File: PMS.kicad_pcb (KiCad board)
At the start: 2 copper layers, 175.5 x 87 mm, 182 parts, among them IC2 SI4459ADY-T1-GE3, IC8 SI4485DY-T1-GE3, J1 XT60-M, J10 XT60-M, J11 CONN_06SILK_FEMALE_PTH, J12 CONN_06SILK_FEMALE_PTH, J13 CONN_06SILK_FEMALE_PTH, J2 XT60-M, J3 Vertical Qwiic Connector, J4 UJ2-MIBH-2-SMT-TR-67, J5 XT60-M, J6 XT60-M, J7 XT60-M, J8 XT60-M, J9 XT60-M, Q1 LTV-8141S, Q10 SI4435DDY, Q11 DMN65D8LFB-7, Q12 SI4435DDY, Q13 DMN65D8LFB-7, Q14 SI4435DDY, Q15 DMN65D8LFB-7, Q16 2N7002PW, Q2 2N7002PW, Q3 DMN65D8LFB-7, Q4 SI4435DDY, Q5 DMN65D8LFB-7, Q6 SI4435DDY, Q7 DMN65D8LFB-7, Q8 SI4435DDY, Q9 DMN65D8LFB-7, T1 TENDA, T2 TENDA, U1 LM35DM, U2 LM2904ITPX/NOPB, U3 LM2904ITPX/NOPB, U4 LM2904ITPX/NOPB, U5 LM2904ITPX/NOPB, U6 LM2904ITPX/NOPB, U7 TLV1117LV33DCYR, U8 LT1374IS8-5PBF

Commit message: PMS V2 Arrangement
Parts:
- moved TETHER0 75.5 mm to (175.8, 139.5)
- moved C33 51.3 mm to (190.8, 139.5), turned to 180 degrees
- moved L2 49.5 mm to (176.5, 128.0), turned to 0 degrees
- moved F1 48.8 mm to (216.0, 138.0), turned to 90 degrees
- moved D4 46.0 mm to (203.5, 138.0), turned to 180 degrees
- moved C32 44.8 mm to (212.0, 137.0)
- moved D5 42.3 mm to (219.5, 130.8), turned to 90 degrees
- moved Q1 41.7 mm to (190.6, 132.0), turned to 180 degrees
- moved U8 39.0 mm to (214.0, 131.0), turned to 180 degrees
- moved C29 35.8 mm to (219.0, 125.5), turned to -90 degrees
- moved C34 33.0 mm to (215.5, 125.5), turned to 180 degrees
- moved C30 32.6 mm to (188.5, 123.0), turned to -90 degrees
- moved C31 30.8 mm to (212.0, 125.5), turned to 90 degrees
- moved L1 30.4 mm to (203.0, 127.0), turned to -90 degrees
- moved R28 29.2 mm to (192.6, 123.0), turned to 90 degrees
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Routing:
- net TRONICS_POWER: track 115.5 -> 185.0 mm, vias 4 -> 2
- net TETHER_A: track 34.5 -> 93.3 mm, vias 0 -> 1
- net +3V3: track 180.9 -> 140.6 mm, vias 1 -> 0
- net TETHER_B: track 54.2 -> 94.1 mm, vias 1 -> 2
- net Net-(Q1-COLLECTOR): track 113.2 -> 152.8 mm, vias 2 -> 4
- net 5V: track 345.6 -> 369.0 mm
- net GND: track 814.1 -> 833.8 mm, vias 17 -> 16
- net Net-(R6-Pad1): track 35.7 -> 51.2 mm
- net Net-(R3-Pad1): track 40.8 -> 48.4 mm, vias 1 -> 0
- net Net-(C30-Pad1): track 15.8 -> 12.3 mm
- net Net-(D5-C): track 9.18 -> 11.9 mm
- net Net-(R5-Pad1): track 39.2 -> 37.9 mm, vias 0 -> 1
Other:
- board size 175.5 x 87 mm -> 163.5 x 87 mm

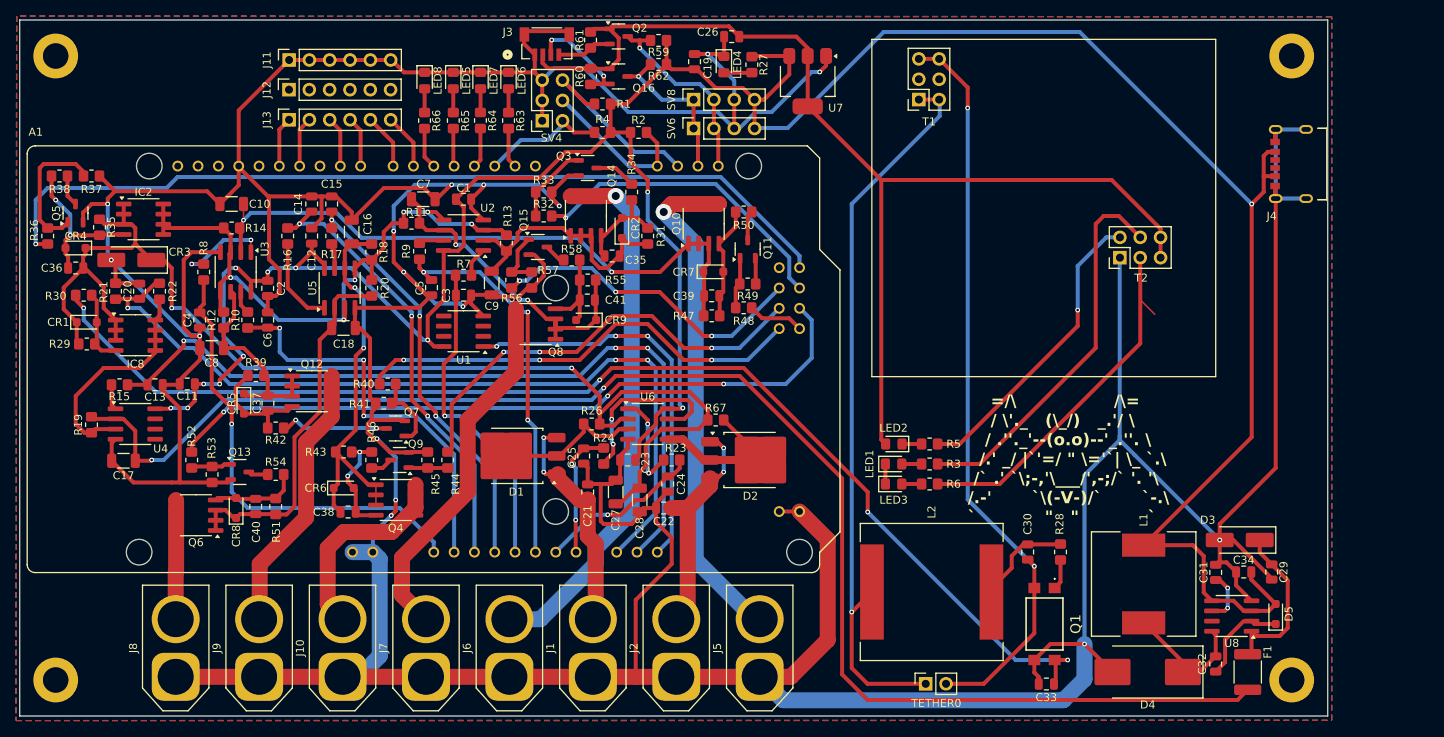
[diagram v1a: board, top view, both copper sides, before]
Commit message: PMS Slim
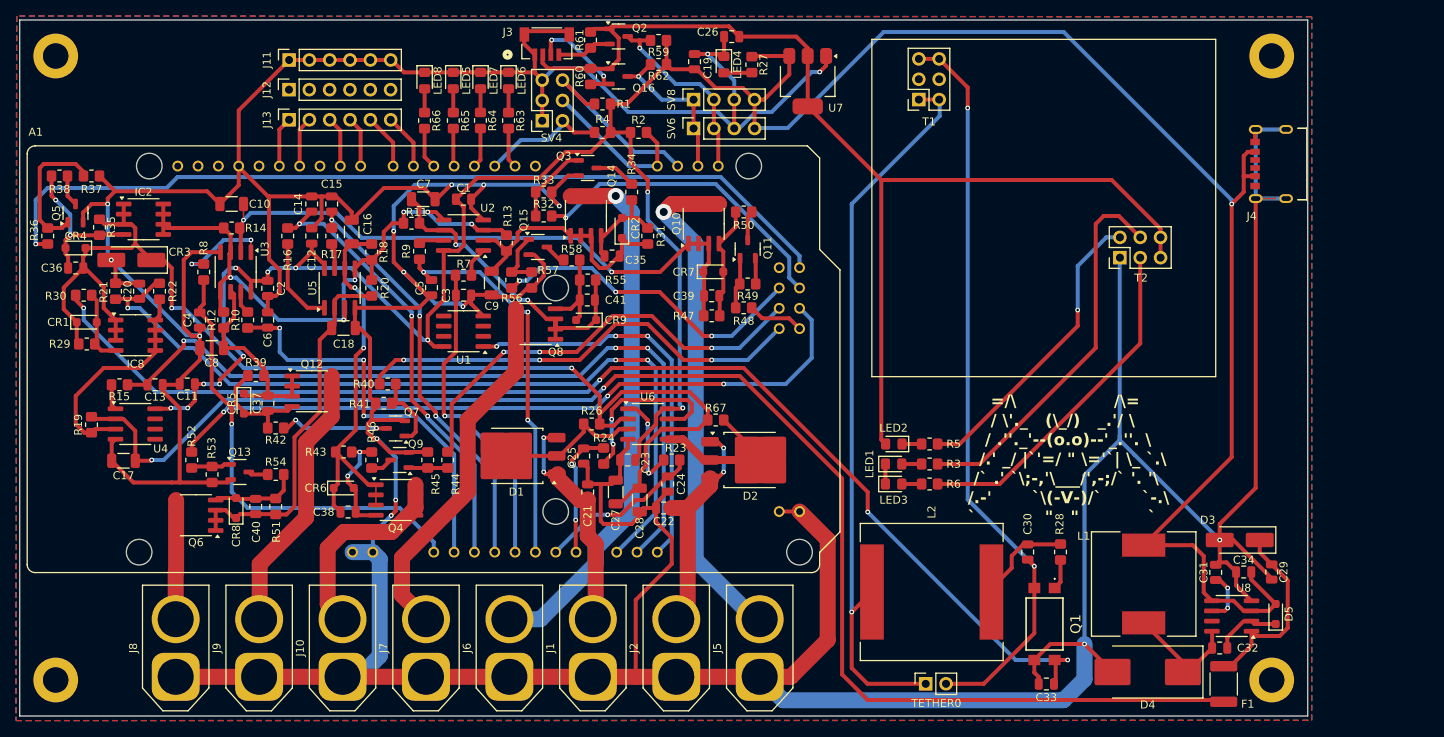
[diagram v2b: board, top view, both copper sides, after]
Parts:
- moved F1 3.35 mm to (213.0, 139.5)
- moved ? 2.50 mm to (219.0, 61.0)
- moved ? 2.50 mm to (219.0, 139.0)
- moved J4 2.50 mm to (220.0, 74.5)
- moved C32 2.06 mm to (212.5, 135.0), turned to 180 degrees
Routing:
- net Net-(R6-Pad1): track 51.2 -> 43.3 mm
- net Net-(D5-C): track 11.9 -> 8.37 mm
- net TRONICS_POWER: track 185.0 -> 181.7 mm
- net Net-(D3-CATHODE): track 20.7 -> 24.0 mm
- net 5V: track 369.0 -> 365.8 mm
- net Net-(D4-K): track 16.4 -> 15.2 mm
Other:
- board size 163.5 x 87 mm -> 161 x 87 mm
